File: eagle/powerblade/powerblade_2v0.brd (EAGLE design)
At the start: 45.7 x 18.4 mm, 91 parts, among them J21 JTAG_14PIN_IDC-NL, J23 AC_INSLOT_OUT, Q1 2N7002, Q2 2N7002, Q3 2N7002, Q4 BF2040, U1 MAX9910, U2 MAX9910, U3 NCS2200S, U4 MSP430FR5738, U5 LP2980, U6 KL02, X1 32.768kHz, X2 32.768kHz, Y1 ANT-USP

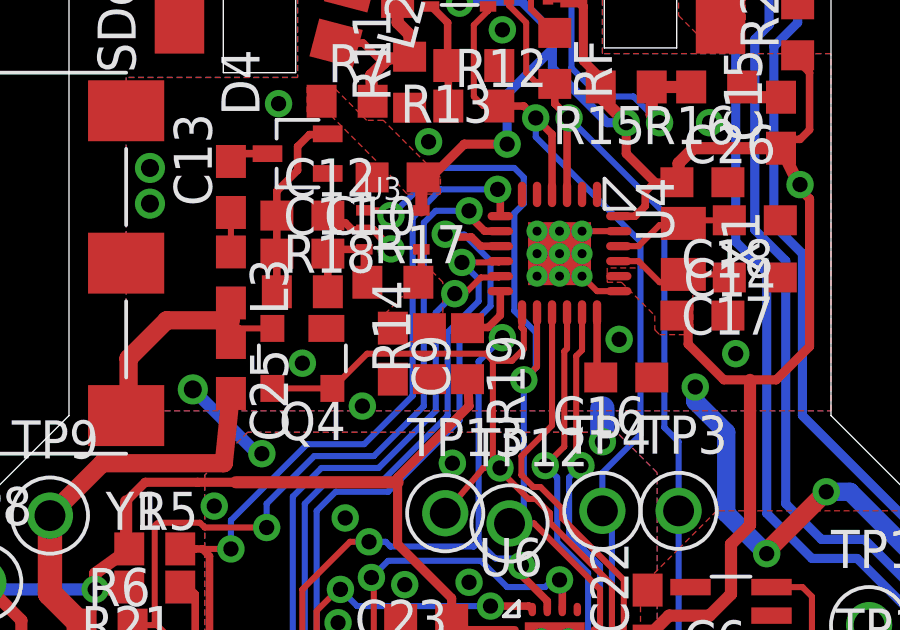
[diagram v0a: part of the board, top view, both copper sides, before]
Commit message: updated to 3 prong ac
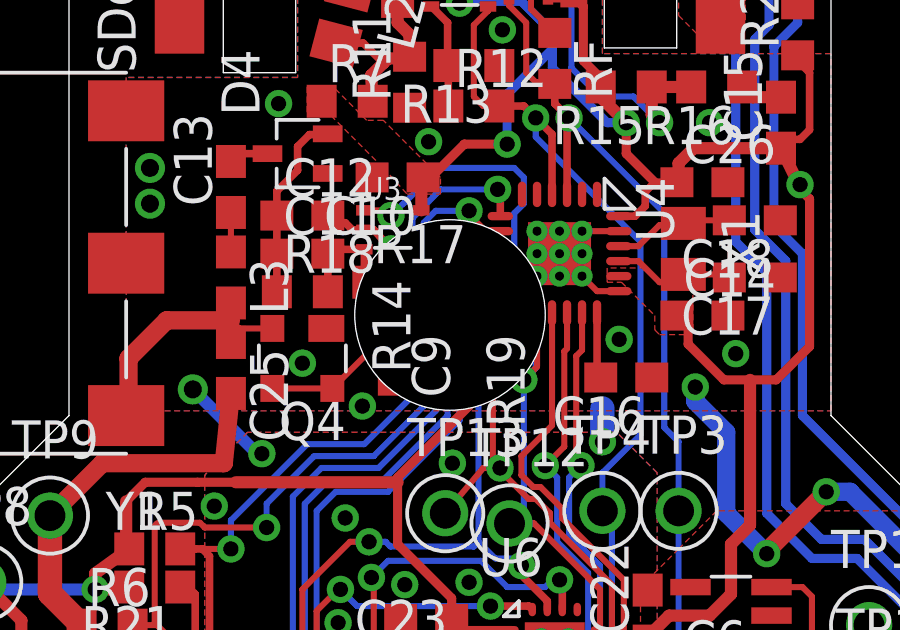
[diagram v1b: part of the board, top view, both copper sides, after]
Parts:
- J23: value AC_INSLOT_OUT -> AC_IN3SLOT_OUT; device powerfilm:AC_SLOT_OUT -> powerfilm:AC3_SLOT_OUT
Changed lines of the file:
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@@
 <attribute name="DIGIKEY" value="NP" x="-6.35" y="-27.94" size="1.778" layer="27" rot="R270" display="off"/>
 </element>
-<element name="J23" library="powerfilm" package="AC_SLOT_OUT" value="AC_INSLOT_OUT" x="0" y="0">
+<element name="J23" library="powerfilm" package="AC3_SLOT_OUT" value="AC_IN3SLOT_OUT" x="0" y="0">
 <attribute name="DIGIKEY" value="3M11307-ND" x="0" y="0" size="1.778" layer="27" display="off"/>
 </element>
@@
 <wire x1="-8.5725" y1="-15.001875" x2="-6.429375" y2="-17.145" width="0.4064" layer="16"/>
 <wire x1="-6.429375" y1="-17.145" x2="-6.270625" y2="-17.145" width="0.4064" layer="16"/>
+<wire x1="-0.6858" y1="-14.66125" x2="-1.905" y2="-14.66125" width="0" layer="19" extent="1-1"/>
+<wire x1="-2.921" y1="-15.5575" x2="-1.905" y2="-14.66125" width="0" layer="19" extent="1-1"/>
+<wire x1="2.90125" y1="-11.2275" x2="2.90125" y2="-10.4775" width="0" layer="19" extent="1-1"/>
+<wire x1="-2.59625" y1="-7.9375" x2="-0.714375" y2="-6.746875" width="0" layer="19" extent="1-1"/>
 </signal>
 <signal name="N$9">
@@
 <vertex x="-2.301875" y="-12.620625"/>
 </polygon>
+<wire x1="-1.905" y1="-12.96125" x2="-0.6858" y2="-12.96125" width="0" layer="19" extent="1-1"/>
+<wire x1="-1.055" y1="-11.43" x2="-0.6858" y2="-12.96125" width="0" layer="19" extent="1-1"/>
 </signal>
 <signal name="RX_BITLINE">
